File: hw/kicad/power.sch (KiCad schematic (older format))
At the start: 60 parts

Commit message: Map INA240 to footprint
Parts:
- removed U? (x2): INA240A2, symbol INA240
- added U? (x2): INA240A2, Housings_SSOP:TSSOP-8_4.4x3mm_Pitch0.65mm, symbol INA240
- U?: footprint (none) -> Housings_SSOP:TSSOP-8_4.4x3mm_Pitch0.65mm
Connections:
- net +3V3: now also U?.5 (VS), U?.5 (VS)
- net GND: now also U?.1 (GND), U?.1 (GND), U?.4 (GND), U?.4 (GND), U?.6 (REF2), U?.6 (REF2)
- net I_SENSE_V_REF: now also U?.7 (REF1), U?.7 (REF1)
- net at R?.3: now also U?.2 (In+) (x2)
- net at R?.4: now also U?.3 (In-) (x2)
- net at R?.1: now also U?.8 (OUT) (x2)
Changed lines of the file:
@@
 F 0 "U?" H 7450 1250 60  0000 C CNN
 F 1 "INA240A2" H 7150 1250 60  0000 C CNN
-F 2 "" H 7250 1500 60  0001 C CNN
+F 2 "Housings_SSOP:TSSOP-8_4.4x3mm_Pitch0.65mm" H 7250 1500 60  0001 C CNN
 F 3 "" H 7250 1500 60  0001 C CNN
 	1    7250 1650
@@
 Text HLabel 9750 2800 2    60   Output ~ 0
 MOT_PH_B
-$Comp
-L INA240 U?
-U 1 1 58272577
-P 7250 3650
-F 0 "U?" H 7450 3250 60  0000 C CNN
-F 1 "INA240A2" H 7150 3250 60  0000 C CNN
-F 2 "" H 7250 3500 60  0001 C CNN
-F 3 "" H 7250 3500 60  0001 C CNN
-	1    7250 3650
-	1    0    0    -1
-$EndComp
 Wire Wire Line
 	7100 3100 7150 3050
@@
 Text HLabel 9750 4800 2    60   Output ~ 0
 MOT_PH_C
-$Comp
-L INA240 U?
-U 1 1 58272855
-P 7250 5650
-F 0 "U?" H 7450 5250 60  0000 C CNN
-F 1 "INA240A2" H 7150 5250 60  0000 C CNN
-F 2 "" H 7250 5500 60  0001 C CNN
-F 3 "" H 7250 5500 60  0001 C CNN
-	1    7250 5650
-	1    0    0    -1
-$EndComp
 Wire Wire Line
 	7100 5100 7150 5050
@@
 	1    0    0    -1
 $EndComp
+$Comp
+L INA240 U?
+U 1 1 58310235
+P 7250 3650
+F 0 "U?" H 7450 3250 60  0000 C CNN
+F 1 "INA240A2" H 7150 3250 60  0000 C CNN
+F 2 "Housings_SSOP:TSSOP-8_4.4x3mm_Pitch0.65mm" H 7250 3500 60  0001 C CNN
+F 3 "" H 7250 3500 60  0001 C CNN
+	1    7250 3650
+	1    0    0    -1
+$EndComp
+$Comp
+L INA240 U?
+U 1 1 5831030C
+P 7250 5650
+F 0 "U?" H 7450 5250 60  0000 C CNN
+F 1 "INA240A2" H 7150 5250 60  0000 C CNN
+F 2 "Housings_SSOP:TSSOP-8_4.4x3mm_Pitch0.65mm" H 7250 5500 60  0001 C CNN
+F 3 "" H 7250 5500 60  0001 C CNN
+	1    7250 5650
+	1    0    0    -1
+$EndComp

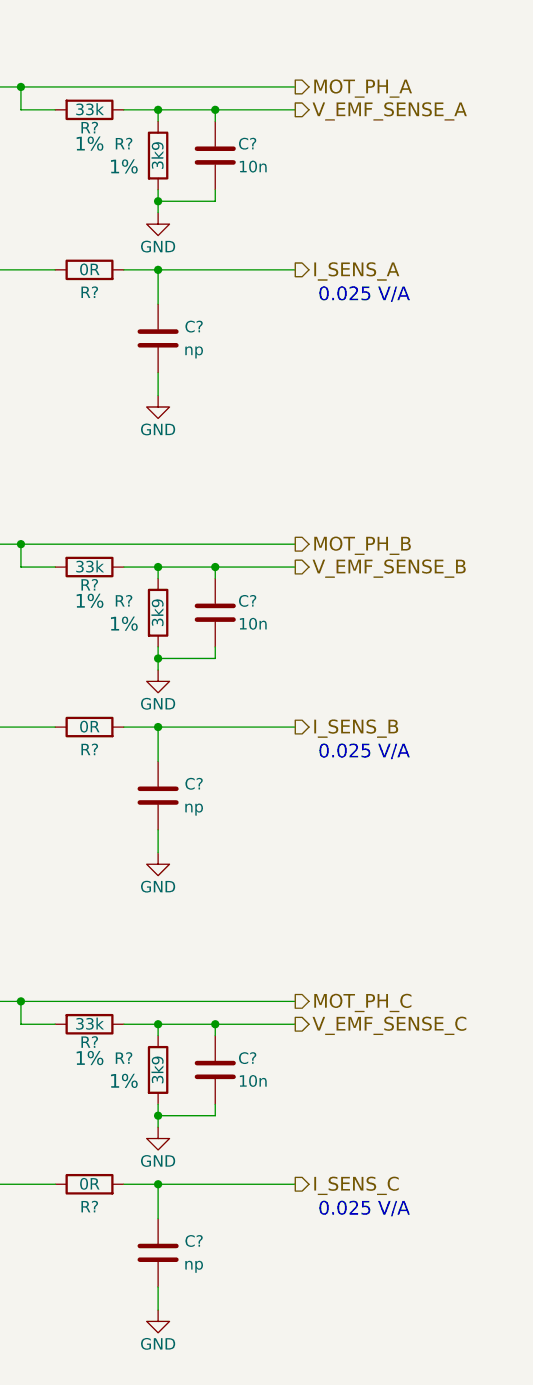
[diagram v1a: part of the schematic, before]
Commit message: Gate power supply enabling and board temp sensor
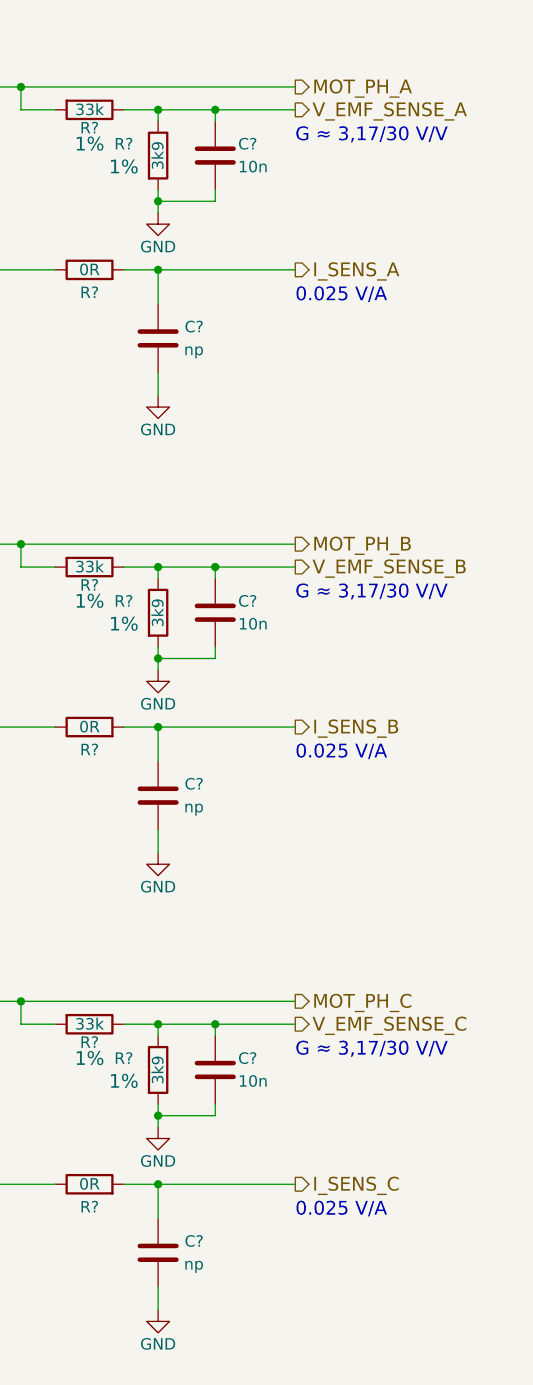
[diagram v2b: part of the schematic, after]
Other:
- note added: "G ≈ 3,17/30 V/V"
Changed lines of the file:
@@
 Text Notes 6950 6200 0    60   ~ 0
 Gain = 50 V/V
-Text Notes 9850 1750 0    60   ~ 0
+Text Notes 9750 1750 0    60   ~ 0
 0.025 V/A
-Text Notes 9850 3750 0    60   ~ 0
+Text Notes 9750 3750 0    60   ~ 0
 0.025 V/A
-Text Notes 9850 5750 0    60   ~ 0
+Text Notes 9750 5750 0    60   ~ 0
 0.025 V/A
 $Comp
@@
 	1    0    0    -1
 $EndComp
+Text Notes 9750 5050 0    60   ~ 0
+G ≈ 3,17/30 V/V
+Text Notes 9750 3050 0    60   ~ 0
+G ≈ 3,17/30 V/V
+Text Notes 9750 1050 0    60   ~ 0
+G ≈ 3,17/30 V/V
 $EndSCHEMATC

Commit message: Annotation
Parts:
- gave numbers to parts that had none: 59

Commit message: Map footprints to components and add BOM
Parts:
- C18, C19, C20: footprint (none) -> Capacitors_SMD:C_0805
- C21, C22, C23, C29, C30, C31, C32, C33, C34, C35, C36, C37, C38, C39, C40: footprint (none) -> Capacitors_SMD:C_0402
- C24, C25, C26: footprint (none) -> Capacitors_SMD:C_0603
- C27, C28, C7: footprint (none) -> Capacitors_SMD:C_1210
- R14, R15, R16, R17, R18, R19, R20, R21, R22, R23, R24, R25, R29, R30, R31, R32, R33, R34, R35, R36, R37: footprint (none) -> Resistors_SMD:R_0402
